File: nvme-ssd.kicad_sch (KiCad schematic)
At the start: 20 parts, among them J3 1-2199230-6

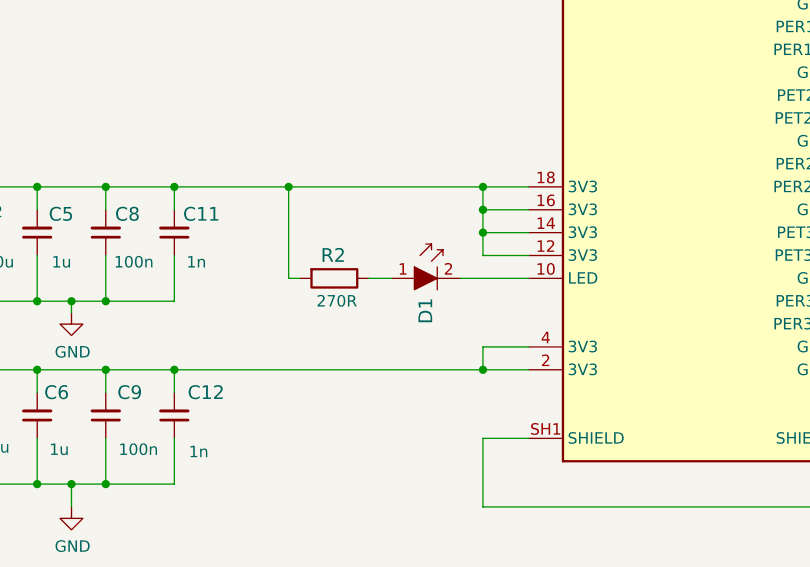
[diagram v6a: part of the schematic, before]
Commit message: Update D1, D11 symbol
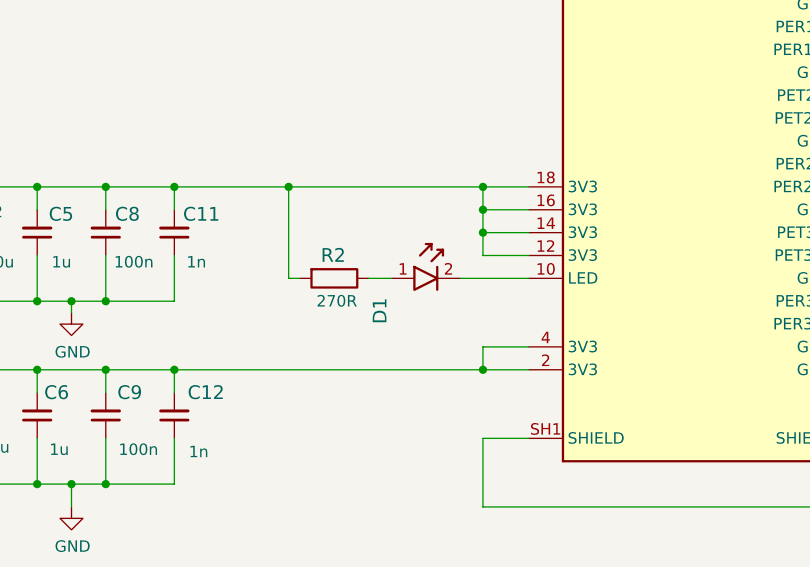
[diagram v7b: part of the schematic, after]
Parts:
- D1: footprint scalenode-cm4-baseboard-footprints:LED_0603_R -> antmicro-footprints:LED_0603_1608Metric_R; symbol scalenode-cm4-baseboard:598-8D80-107F -> antmicroLEDIndicationDiscrete:598-8D80-107F; Author (none) -> Antmicro; License (none) -> Apache-2.0
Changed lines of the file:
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@@
     (pin "2")
   )
-  (symbol (lib_id "scalenode-cm4-baseboard:598-8D80-107F") (at 123.19 123.19 0) (unit 1)
+  (symbol (lib_id "antmicroLEDIndicationDiscrete:598-8D80-107F") (at 118.11 123.19 0) (unit 1)
     (in_bom yes) (on_board yes)
-    (property "Reference" "D1" (id 0) (at 121.92 128.27 90)
+    (property "Reference" "D1" (id 0) (at 116.84 128.27 90)
       (effects (font (size 1.524 1.524)) (justify left))
     )
-    (property "Value" "598-8D80-107F" (id 1) (at 123.2662 118.6688 90)
+    (property "Value" "598-8D80-107F" (id 1) (at 118.1862 118.6688 90)
       (effects (font (size 1.524 1.524)) (justify left) hide)
     )
-    (property "Footprint" "scalenode-cm4-baseboard-footprints:LED_0603_R" (id 2) (at 128.27 118.11 0)
-      (effects (font (size 1.524 1.524)) (justify left) hide)
+    (property "Footprint" "antmicro-footprints:LED_0603_1608Metric_R" (id 2) (at 140.97 130.81 0)
+      (effects (font (size 1.27 1.27) (thickness 0.15)) (justify left bottom) hide)
     )
-    (property "Datasheet" "" (id 3) (at 128.27 115.57 0)
-      (effects (font (size 1.524 1.524)) (justify left) hide)
+    (property "Datasheet" "" (id 3) (at 140.97 133.35 0)
+      (effects (font (size 1.27 1.27) (thickness 0.15)) (justify left bottom) hide)
     )
-    (property "MPN" "598-8D80-107F" (id 4) (at 128.27 110.49 0)
-      (effects (font (size 1.524 1.524)) (justify left) hide)
+    (property "MPN" "598-8D80-107F" (id 4) (at 140.97 135.89 0)
+      (effects (font (size 1.27 1.27) (thickness 0.15)) (justify left bottom) hide)
     )
-    (property "Manufacturer" "DIALIGHT" (id 5) (at 128.524 107.442 0)
-      (effects (font (size 1.524 1.524)) (justify left) hide)
+    (property "Manufacturer" "DIALIGHT" (id 5) (at 140.97 138.43 0)
+      (effects (font (size 1.27 1.27) (thickness 0.15)) (justify left bottom) hide)
+    )
+    (property "Author" "Antmicro" (id 6) (at 140.97 140.97 0)
+      (effects (font (size 1.27 1.27) (thickness 0.15)) (justify left bottom) hide)
+    )
+    (property "License" "Apache-2.0" (id 7) (at 140.97 143.51 0)
+      (effects (font (size 1.27 1.27) (thickness 0.15)) (justify left bottom) hide)
     )
     (pin "1")
